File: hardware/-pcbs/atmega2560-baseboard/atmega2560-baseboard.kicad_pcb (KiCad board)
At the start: 2 copper layers, 18 parts, among them J1 Bottom, SW1 SW_Push, U1 ATMEGA2560-16AU, Y1 16MHz

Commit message: Spread out all footprints
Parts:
- moved C1 51.7 mm to (200.1, 106.2)
- moved C5 48.8 mm to (195.9, 116.3)
- moved R1 47.8 mm to (195.8, 111.5)
- moved R6 47.4 mm to (195.8, 106.4)
- moved C4 43.3 mm to (190.1, 117.0)
- moved Y1 42.4 mm to (184.6, 127.1)
- moved C2 41.2 mm to (186.0, 122.0)
- moved R2 39.3 mm to (185.9, 117.2)
- moved C3 38.6 mm to (180.1, 127.2)
- moved D2 37.9 mm to (168.0, 137.5)
- moved SW1 37.0 mm to (185.4, 107.0)
- moved D3 36.4 mm to (172.4, 132.4)
- moved D1 35.6 mm to (176.2, 127.3)
- moved R3 33.7 mm to (168.0, 132.4)
- moved R4 32.7 mm to (172.4, 127.4)
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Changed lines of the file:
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@@
   (general
     (links 62)
-    (no_connects 47)
+    (no_connects 62)
     (area 0 0 0 0)
     (thickness 1.6)
@@
   )
   (module Capacitors_SMD:C_0603_HandSoldering (layer F.Cu)
-    (at 148.5011 105.0036)
+    (at 200.146571 106.238)
     (descr "Capacitor SMD 0603, hand soldering")
     (tags "capacitor 0603")
@@
   )
   (module Capacitors_SMD:C_0603_HandSoldering (layer F.Cu)
-    (at 148.5011 105.0036)
+    (at 185.979428 122.038)
     (descr "Capacitor SMD 0603, hand soldering")
     (tags "capacitor 0603")
@@
   )
   (module Capacitors_SMD:C_0603_HandSoldering (layer F.Cu)
-    (at 148.5011 105.0036)
+    (at 180.099428 127.188)
     (descr "Capacitor SMD 0603, hand soldering")
     (tags "capacitor 0603")
@@
   )
   (module Capacitors_SMD:C_0603_HandSoldering (layer F.Cu)
-    (at 148.5011 105.0036)
+    (at 190.093001 116.988)
     (descr "Capacitor SMD 0603, hand soldering")
     (tags "capacitor 0603")
@@
   )
   (module Capacitors_SMD:C_0603_HandSoldering (layer F.Cu)
-    (at 148.5011 105.0036)
+    (at 195.929428 116.338)
     (descr "Capacitor SMD 0603, hand soldering")
     (tags "capacitor 0603")
@@
   )
   (module Diodes_SMD:D_0603 (layer F.Cu)
-    (at 148.5011 105.0036)
+    (at 176.203001 127.338)
     (descr "Diode SMD in 0603 package http://datasheets.avx.com/schottky.pdf")
     (tags "smd diode")
@@
   )
   (module LEDs:LED_0603_HandSoldering (layer F.Cu)
-    (at 148.5011 105.0036)
+    (at 168.043001 137.488)
     (descr "LED SMD 0603, hand soldering")
     (tags "LED 0603")
@@
   )
   (module LEDs:LED_0603_HandSoldering (layer F.Cu)
-    (at 148.5011 105.0036)
+    (at 172.403001 132.438)
     (descr "LED SMD 0603, hand soldering")
     (tags "LED 0603")
@@
   )
   (module Pin_Headers:Pin_Header_Straight_2x12_Pitch2.54mm (layer F.Cu)
-    (at 148.5011 105.0036)
+    (at 161.283001 107.318)
     (descr "Through hole straight pin header, 2x12, 2.54mm pitch, double rows")
     (tags "Through hole pin header THT 2x12 2.54mm double row")
@@
   )
   (module Resistors_SMD:R_0603_HandSoldering (layer F.Cu)
-    (at 148.5011 105.0036)
+    (at 195.843001 111.488)
     (descr "Resistor SMD 0603, hand soldering")
     (tags "resistor 0603")
@@
   )
   (module Resistors_SMD:R_0603_HandSoldering (layer F.Cu)
-    (at 148.5011 105.0036)
+    (at 185.893001 117.188)
     (descr "Resistor SMD 0603, hand soldering")
     (tags "resistor 0603")
@@
   )
   (module Resistors_SMD:R_0603_HandSoldering (layer F.Cu)
-    (at 148.5011 105.0036)
+    (at 168.043001 132.438)
     (descr "Resistor SMD 0603, hand soldering")
     (tags "resistor 0603")
@@
   )
   (module Resistors_SMD:R_0603_HandSoldering (layer F.Cu)
-    (at 148.5011 105.0036)
+    (at 172.403001 127.388)
     (descr "Resistor SMD 0603, hand soldering")
     (tags "resistor 0603")
@@
   )
   (module Resistors_SMD:R_0603_HandSoldering (layer F.Cu)
-    (at 148.5011 105.0036)
+    (at 168.043001 127.388)
     (descr "Resistor SMD 0603, hand soldering")
     (tags "resistor 0603")
@@
   )
   (module Resistors_SMD:R_0603_HandSoldering (layer F.Cu)
-    (at 148.5011 105.0036)
+    (at 195.843001 106.438)
     (descr "Resistor SMD 0603, hand soldering")
     (tags "resistor 0603")
@@
   )
   (module Buttons_Switches_THT:SW_PUSH_6mm (layer F.Cu)
-    (at 148.5011 105.0036)
+    (at 185.433001 106.988)
     (descr https://www.omron.com/ecb/products/pdf/en-b3f.pdf)
     (tags "tact sw push 6mm")
@@
   )
   (module Housings_QFP:TQFP-100_14x14mm_Pitch0.5mm (layer F.Cu)
-    (at 148.5011 105.0036)
+    (at 174.783001 114.438)
     (descr "100-Lead Plastic Thin Quad Flatpack (PF) - 14x14x1 mm Body 2.00 mm Footprint [TQFP] (see Microchip Packaging Specification 00000049BS.pdf)")
     (tags "QFP 0.5")
@@
   )
   (module CSTCE16M0V53-R0:OSC_CSTCE16M0V53-R0 (layer F.Cu)
-    (at 148.5011 105.0036)
+    (at 184.631501 127.138116)
     (attr smd)
     (fp_text reference Y1 (at -0.882758 -1.61337) (layer F.SilkS)

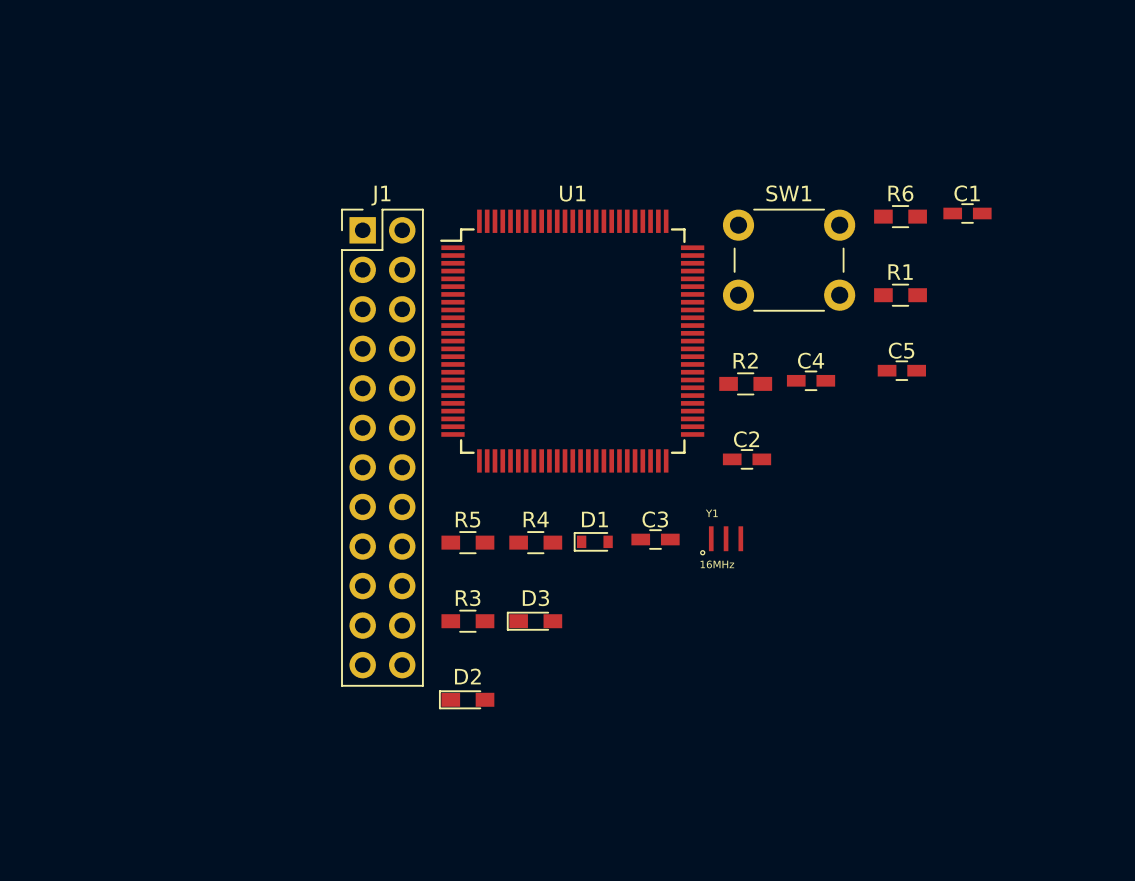
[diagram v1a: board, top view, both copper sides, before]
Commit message: Route VCC and GND pin
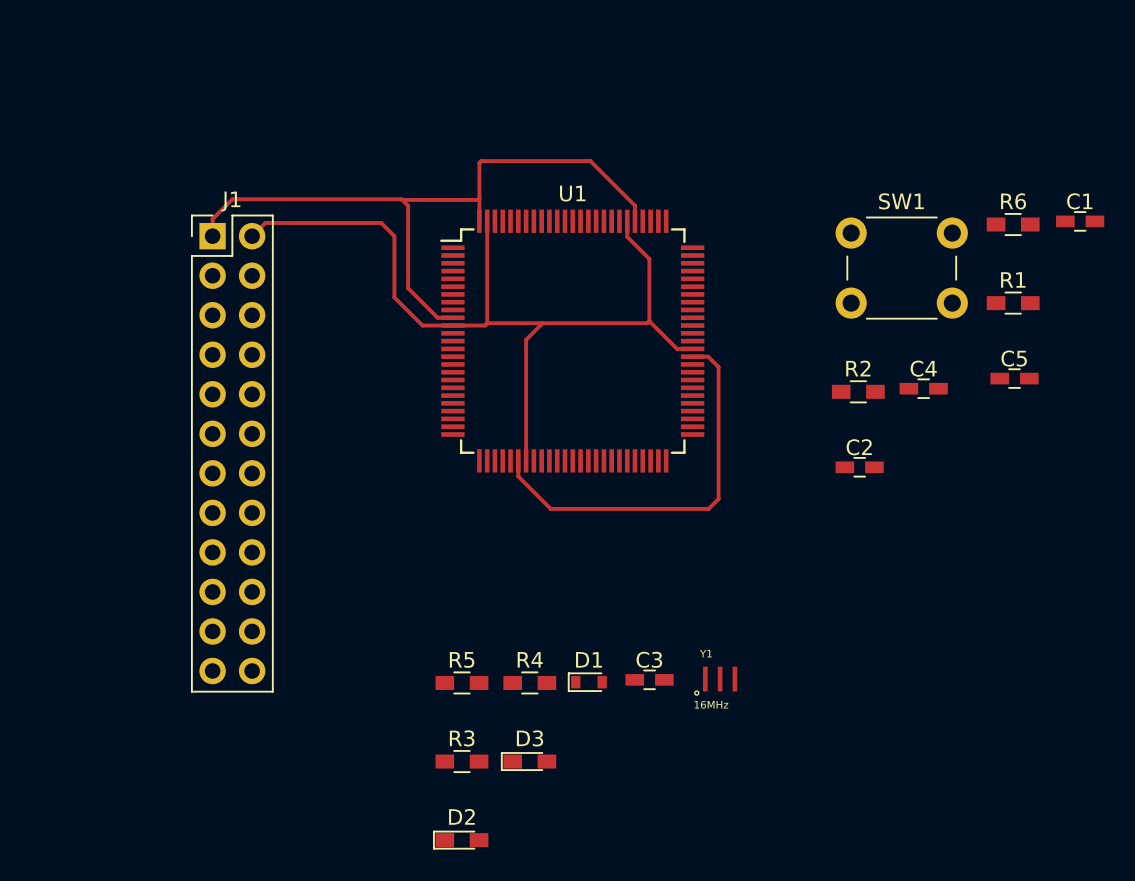
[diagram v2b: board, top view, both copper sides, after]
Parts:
- moved J1 9.65 mm to (151.6, 107.7)
- moved D3 9.03 mm to (172.0, 141.5)
- moved R3 9.03 mm to (167.7, 141.5)
- moved C3 9.03 mm to (179.7, 136.2)
- moved D1 9.03 mm to (175.8, 136.4)
- moved D2 9.03 mm to (167.7, 146.5)
- moved R4 9.03 mm to (172.0, 136.4)
- moved R5 9.03 mm to (167.7, 136.4)
- moved Y1 9.03 mm to (184.3, 136.2)
- moved C1 7.26 mm to (207.4, 106.7)
- moved C4 7.26 mm to (197.3, 117.5)
- moved C5 7.26 mm to (203.2, 116.8)
- moved R1 7.26 mm to (203.1, 112.0)
- moved R2 7.26 mm to (193.1, 117.7)
- moved R6 7.26 mm to (203.1, 106.9)
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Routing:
- net +5V: track 0.00 -> 69.7 mm
- net GND: track 0.00 -> 57.4 mm
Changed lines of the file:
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@@
   (general
     (links 62)
-    (no_connects 62)
-    (area 0 0 0 0)
+    (no_connects 61)
+    (area 149.612999 102.544999 209.514143 149.13)
     (thickness 1.6)
     (drawings 0)
-    (tracks 0)
+    (tracks 42)
     (zones 0)
     (modules 18)
@@
     (pad_to_mask_clearance 0)
     (aux_axis_origin 0 0)
-    (visible_elements FFFFFF7F)
+    (visible_elements FFFFE77F)
     (pcbplotparams
       (layerselection 0x00030_80000001)
@@
   )
   (module Capacitors_SMD:C_0603_HandSoldering (layer F.Cu)
-    (at 200.146571 106.238)
+    (at 207.385571 106.746)
     (descr "Capacitor SMD 0603, hand soldering")
     (tags "capacitor 0603")
@@
   )
   (module Capacitors_SMD:C_0603_HandSoldering (layer F.Cu)
-    (at 185.979428 122.038)
+    (at 193.218428 122.546)
     (descr "Capacitor SMD 0603, hand soldering")
     (tags "capacitor 0603")
@@
   )
   (module Capacitors_SMD:C_0603_HandSoldering (layer F.Cu)
-    (at 180.099428 127.188)
+    (at 179.718428 136.205)
     (descr "Capacitor SMD 0603, hand soldering")
     (tags "capacitor 0603")
@@
   )
   (module Capacitors_SMD:C_0603_HandSoldering (layer F.Cu)
-    (at 190.093001 116.988)
+    (at 197.332001 117.496)
     (descr "Capacitor SMD 0603, hand soldering")
     (tags "capacitor 0603")
@@
   )
   (module Capacitors_SMD:C_0603_HandSoldering (layer F.Cu)
-    (at 195.929428 116.338)
+    (at 203.168428 116.846)
     (descr "Capacitor SMD 0603, hand soldering")
     (tags "capacitor 0603")
@@
   )
   (module Diodes_SMD:D_0603 (layer F.Cu)
-    (at 176.203001 127.338)
+    (at 175.822001 136.355)
     (descr "Diode SMD in 0603 package http://datasheets.avx.com/schottky.pdf")
     (tags "smd diode")
@@
   )
   (module LEDs:LED_0603_HandSoldering (layer F.Cu)
-    (at 168.043001 137.488)
+    (at 167.662001 146.505)
     (descr "LED SMD 0603, hand soldering")
     (tags "LED 0603")
@@
   )
   (module LEDs:LED_0603_HandSoldering (layer F.Cu)
-    (at 172.403001 132.438)
+    (at 172.022001 141.455)
     (descr "LED SMD 0603, hand soldering")
     (tags "LED 0603")
@@
   )
   (module Pin_Headers:Pin_Header_Straight_2x12_Pitch2.54mm (layer F.Cu)
-    (at 161.283001 107.318)
+    (at 151.638 107.696)
     (descr "Through hole straight pin header, 2x12, 2.54mm pitch, double rows")
     (tags "Through hole pin header THT 2x12 2.54mm double row")
@@
   )
   (module Resistors_SMD:R_0603_HandSoldering (layer F.Cu)
-    (at 195.843001 111.488)
+    (at 203.082001 111.996)
     (descr "Resistor SMD 0603, hand soldering")
     (tags "resistor 0603")
@@
   )
   (module Resistors_SMD:R_0603_HandSoldering (layer F.Cu)
-    (at 185.893001 117.188)
+    (at 193.132001 117.696)
     (descr "Resistor SMD 0603, hand soldering")
     (tags "resistor 0603")
@@
   )
   (module Resistors_SMD:R_0603_HandSoldering (layer F.Cu)
-    (at 168.043001 132.438)
+    (at 167.662001 141.455)
     (descr "Resistor SMD 0603, hand soldering")
     (tags "resistor 0603")
@@
   )
   (module Resistors_SMD:R_0603_HandSoldering (layer F.Cu)
-    (at 172.403001 127.388)
+    (at 172.022001 136.405)
     (descr "Resistor SMD 0603, hand soldering")
     (tags "resistor 0603")
@@
   )
   (module Resistors_SMD:R_0603_HandSoldering (layer F.Cu)
-    (at 168.043001 127.388)
+    (at 167.662001 136.405)
     (descr "Resistor SMD 0603, hand soldering")
     (tags "resistor 0603")
@@
   )
   (module Resistors_SMD:R_0603_HandSoldering (layer F.Cu)
-    (at 195.843001 106.438)
+    (at 203.082001 106.946)
     (descr "Resistor SMD 0603, hand soldering")
     (tags "resistor 0603")
@@
   )
   (module Buttons_Switches_THT:SW_PUSH_6mm (layer F.Cu)
-    (at 185.433001 106.988)
+    (at 192.672001 107.496)
     (descr https://www.omron.com/ecb/products/pdf/en-b3f.pdf)
     (tags "tact sw push 6mm")
@@
   )
   (module CSTCE16M0V53-R0:OSC_CSTCE16M0V53-R0 (layer F.Cu)
-    (at 184.631501 127.138116)
+    (at 184.250501 136.155116)
     (attr smd)
     (fp_text reference Y1 (at -0.882758 -1.61337) (layer F.SilkS)
@@
       (net 45 /XTAL2))
   )
+  (segment (start 163.322 111.633) (end 165.127 113.438) (width 0.25) (layer F.Cu) (net 2))
+  (segment (start 165.127 113.438) (end 167.083001 113.438) (width 0.25) (layer F.Cu) (net 2))
+  (segment (start 163.322 107.696) (end 163.322 111.633) (width 0.25) (layer F.Cu) (net 2))
+  (segment (start 162.472001 106.846001) (end 163.322 107.696) (width 0.25) (layer F.Cu) (net 2))
+  (segment (start 154.178 107.696) (end 155.027999 106.846001) (width 0.25) (layer F.Cu) (net 2))
+  (segment (start 155.027999 106.846001) (end 162.472001 106.846001) (width 0.25) (layer F.Cu) (net 2))
+  (segment (start 169.283001 113.291999) (end 172.847 113.291999) (width 0.25) (layer F.Cu) (net 2))
+  (segment (start 172.847 113.291999) (end 179.573 113.291999) (width 0.25) (layer F.Cu) (net 2))
+  (segment (start 171.783001 122.138) (end 171.783001 114.355998) (width 0.25) (layer F.Cu) (net 2))
+  (segment (start 171.783001 114.355998) (end 172.847 113.291999) (width 0.25) (layer F.Cu) (net 2))
+  (segment (start 179.573 113.291999) (end 179.705 113.159999) (width 0.25) (layer F.Cu) (net 2))
+  (segment (start 179.705 109.159999) (end 179.705 113.159999) (width 0.25) (layer F.Cu) (net 2))
+  (segment (start 181.483001 114.938) (end 182.483001 114.938) (width 0.25) (layer F.Cu) (net 2))
+  (segment (start 179.705 113.159999) (end 181.483001 114.938) (width 0.25) (layer F.Cu) (net 2))
+  (segment (start 178.283001 106.738) (end 178.283001 107.738) (width 0.25) (layer F.Cu) (net 2))
+  (segment (start 178.283001 107.738) (end 179.705 109.159999) (width 0.25) (layer F.Cu) (net 2))
+  (segment (start 169.137 113.438) (end 169.283001 113.291999) (width 0.25) (layer F.Cu) (net 2))
+  (segment (start 169.283001 113.291999) (end 169.283001 106.738) (width 0.25) (layer F.Cu) (net 2))
+  (segment (start 167.083001 113.438) (end 169.137 113.438) (width 0.25) (layer F.Cu) (net 2))
+  (segment (start 166.097998 112.938) (end 167.083001 112.938) (width 0.25) (layer F.Cu) (net 3))
+  (segment (start 164.201002 111.041004) (end 166.097998 112.938) (width 0.25) (layer F.Cu) (net 3))
+  (segment (start 164.201002 105.740002) (end 164.201002 111.041004) (width 0.25) (layer F.Cu) (net 3))
+  (segment (start 163.83 105.369) (end 164.201002 105.740002) (width 0.25) (layer F.Cu) (net 3))
+  (segment (start 183.515 125.222) (end 173.367001 125.222) (width 0.25) (layer F.Cu) (net 3))
+  (segment (start 173.367001 125.222) (end 171.283001 123.138) (width 0.25) (layer F.Cu) (net 3))
+  (segment (start 171.283001 123.138) (end 171.283001 122.138) (width 0.25) (layer F.Cu) (net 3))
+  (segment (start 184.15 124.587) (end 183.515 125.222) (width 0.25) (layer F.Cu) (net 3))
+  (segment (start 184.15 116.104999) (end 184.15 124.587) (width 0.25) (layer F.Cu) (net 3))
+  (segment (start 182.483001 115.438) (end 183.483001 115.438) (width 0.25) (layer F.Cu) (net 3))
+  (segment (start 183.483001 115.438) (end 184.15 116.104999) (width 0.25) (layer F.Cu) (net 3))
+  (segment (start 168.783001 102.996999) (end 168.783001 105.283) (width 0.25) (layer F.Cu) (net 3))
+  (segment (start 168.783001 105.283) (end 168.783001 106.738) (width 0.25) (layer F.Cu) (net 3))
+  (segment (start 163.83 105.369) (end 168.697001 105.369) (width 0.25) (layer F.Cu) (net 3))
+  (segment (start 168.697001 105.369) (end 168.783001 105.283) (width 0.25) (layer F.Cu) (net 3))
+  (segment (start 168.91 102.87) (end 168.783001 102.996999) (width 0.25) (layer F.Cu) (net 3))
+  (segment (start 175.915001 102.87) (end 168.91 102.87) (width 0.25) (layer F.Cu) (net 3))
+  (segment (start 178.783001 106.738) (end 178.783001 105.738) (width 0.25) (layer F.Cu) (net 3))
+  (segment (start 178.783001 105.738) (end 175.915001 102.87) (width 0.25) (layer F.Cu) (net 3))
+  (segment (start 151.638 107.696) (end 151.638 106.596) (width 0.25) (layer F.Cu) (net 3))
+  (segment (start 151.638 106.596) (end 152.908 105.326) (width 0.25) (layer F.Cu) (net 3))
+  (segment (start 152.908 105.326) (end 163.787 105.326) (width 0.25) (layer F.Cu) (net 3))
+  (segment (start 163.787 105.326) (end 163.83 105.369) (width 0.25) (layer F.Cu) (net 3))
 )

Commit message: Route basic pins
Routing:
- net /SCL: track 0.00 -> 34.9 mm, vias 0 -> 2
- net /SDA: track 0.00 -> 33.9 mm, vias 0 -> 2
- net /AREF: track 0.00 -> 29.7 mm, vias 0 -> 2
- net /RESET: track 0.00 -> 26.3 mm
- net /RX0: track 0.00 -> 22.8 mm, vias 0 -> 2
- net /SCK: track 0.00 -> 19.1 mm, vias 0 -> 2
- net /MOSI: track 0.00 -> 17.8 mm, vias 0 -> 2
- net /MISO: track 0.00 -> 16.9 mm, vias 0 -> 2
- net /TX0: track 0.00 -> 15.8 mm, vias 0 -> 2
- net +5V: track 69.7 -> 72.7 mm
